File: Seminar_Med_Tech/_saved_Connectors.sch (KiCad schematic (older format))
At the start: 12 parts

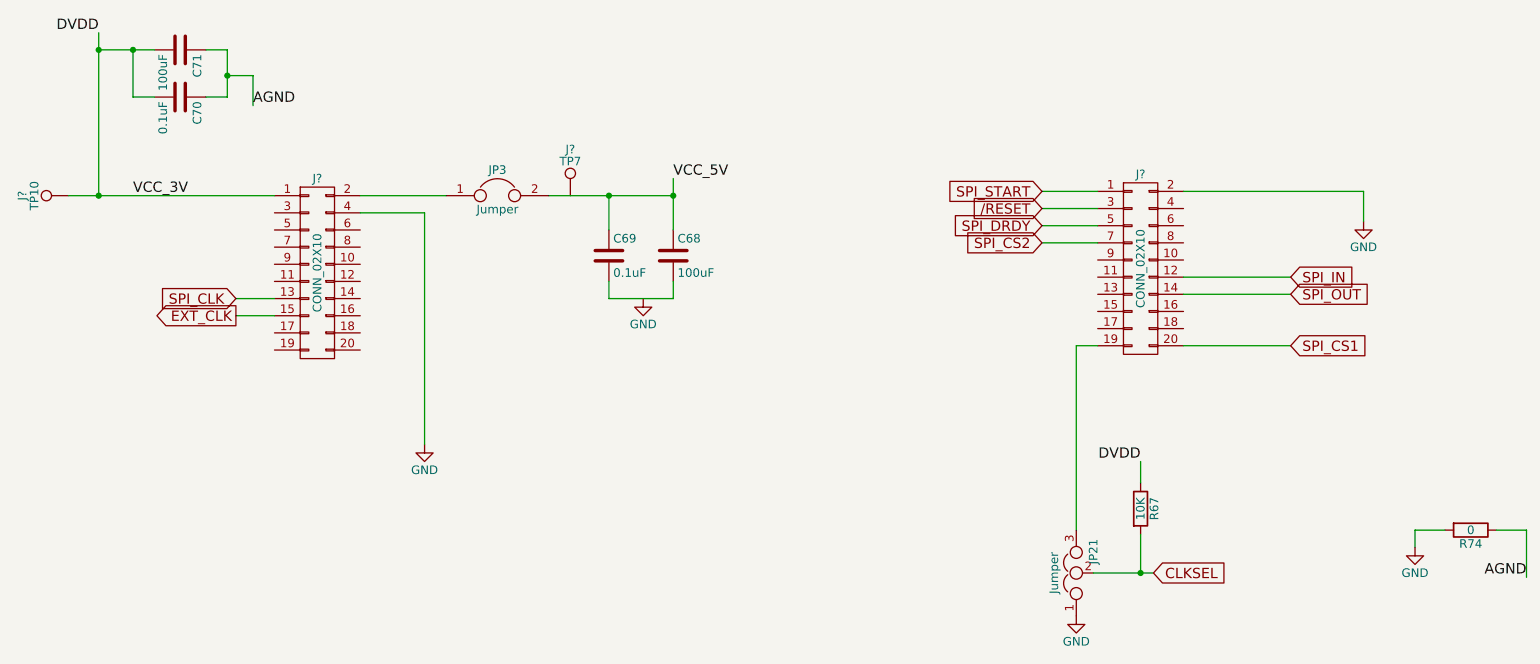
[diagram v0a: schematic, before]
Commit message: Changed labels
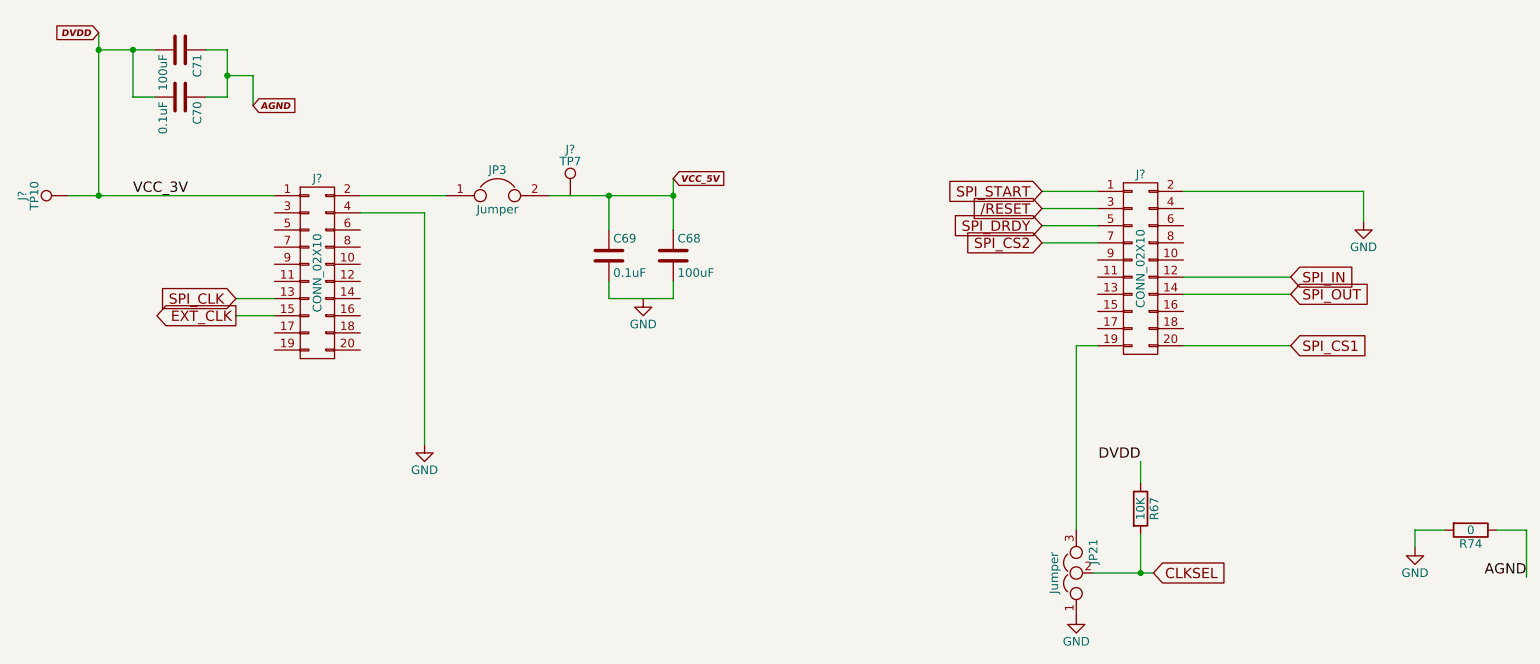
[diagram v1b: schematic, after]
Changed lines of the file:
@@
 EESchema Schematic File Version 2
+LIBS:Seminar_Med_Tech-rescue
 LIBS:power
 LIBS:device
@@
 LIBS:contrib
 LIBS:valves
-LIBS:ECG_Power_Supplies-cache
 LIBS:MechTech
+LIBS:MedTech
 LIBS:MedTec2
-LIBS:MedTech
-LIBS:Seminar_Med_Tech 4-cache
 LIBS:Seminar_Med_Tech-cache
-LIBS:Seminar_Med_Tech-rescue
-LIBS:Connectors-cache
 EELAYER 25 0
 EELAYER END
 $Descr A4 11693 8268
 encoding utf-8
-Sheet 1 1
+Sheet 2 3
 Title ""
 Date ""
@@
 	0    -1   -1   0
 $EndComp
-Text Label 1525 2600 2    60   ~ 0
-DVDD
 $Comp
 L C C71
@@
 	0    1    1    0
 $EndComp
-Text Label 2425 3025 0    60   ~ 0
-AGND
 $Comp
 L Jumper JP3
@@
 Text Label 1725 3550 0    60   ~ 0
 VCC_3V
-Text Label 4875 3450 0    60   ~ 0
-VCC_5V
 Wire Wire Line
 	2550 4150 2325 4150
@@
 	2325 4250 2550 4250
 Wire Wire Line
-	7325 5750 7600 5750
-Wire Wire Line
-	7600 5750 7675 5750
+	7325 5750 7675 5750
 Wire Wire Line
 	7600 5525 7600 5750
@@
 	9850 5500 9850 5775
 Wire Wire Line
-	1350 3550 1525 3550
-Wire Wire Line
-	1525 3550 2550 3550
-Wire Wire Line
-	1525 2600 1525 2700
-Wire Wire Line
-	1525 2700 1525 3550
+	1350 3550 2550 3550
+Wire Wire Line
+	1525 2600 1525 3550
 Connection ~ 1525 3550
 Wire Wire Line
-	1525 2700 1725 2700
-Wire Wire Line
-	1725 2700 1850 2700
+	1525 2700 1850 2700
 Connection ~ 1525 2700
 Wire Wire Line
@@
 	2150 2700 2275 2700
 Wire Wire Line
-	2275 2700 2275 2850
-Wire Wire Line
-	2275 2850 2275 2975
+	2275 2700 2275 2975
 Wire Wire Line
 	2275 2975 2150 2975
@@
 	3050 3550 3550 3550
 Wire Wire Line
-	4150 3550 4500 3550
-Wire Wire Line
-	4500 3550 4875 3550
-Wire Wire Line
-	4875 3450 4875 3550
-Wire Wire Line
-	4875 3550 4875 3750
+	4150 3550 4875 3550
+Wire Wire Line
+	4875 3450 4875 3750
 Wire Wire Line
 	4500 3750 4500 3550
@@
 	4875 4150 4875 4050
 Connection ~ 4875 3550
+Text GLabel 1525 2600 0    39   Input Italic 8
+DVDD
+Text GLabel 2425 3025 2    39   Input Italic 8
+AGND
+Text GLabel 4875 3450 2    39   Input Italic 8
+VCC_5V
 $EndSCHEMATC
